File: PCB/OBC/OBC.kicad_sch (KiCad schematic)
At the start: 1 part, among them U1 STM32F405RGTx

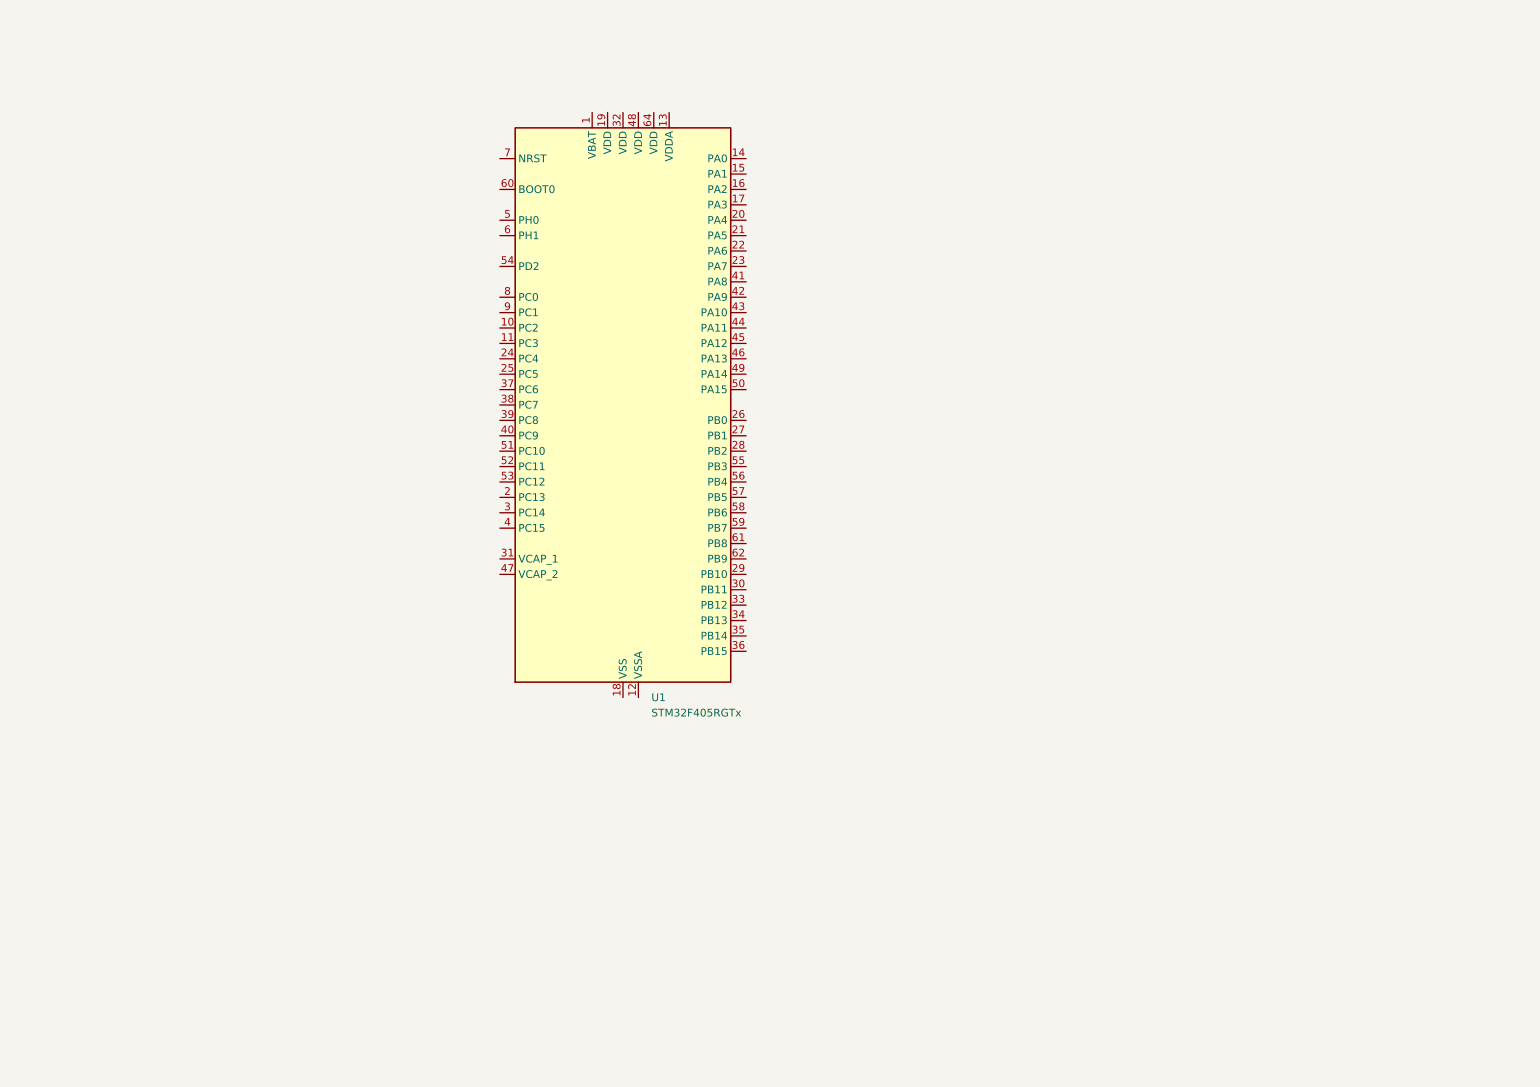
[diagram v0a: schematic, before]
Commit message: Adding LDO and Stm32F4
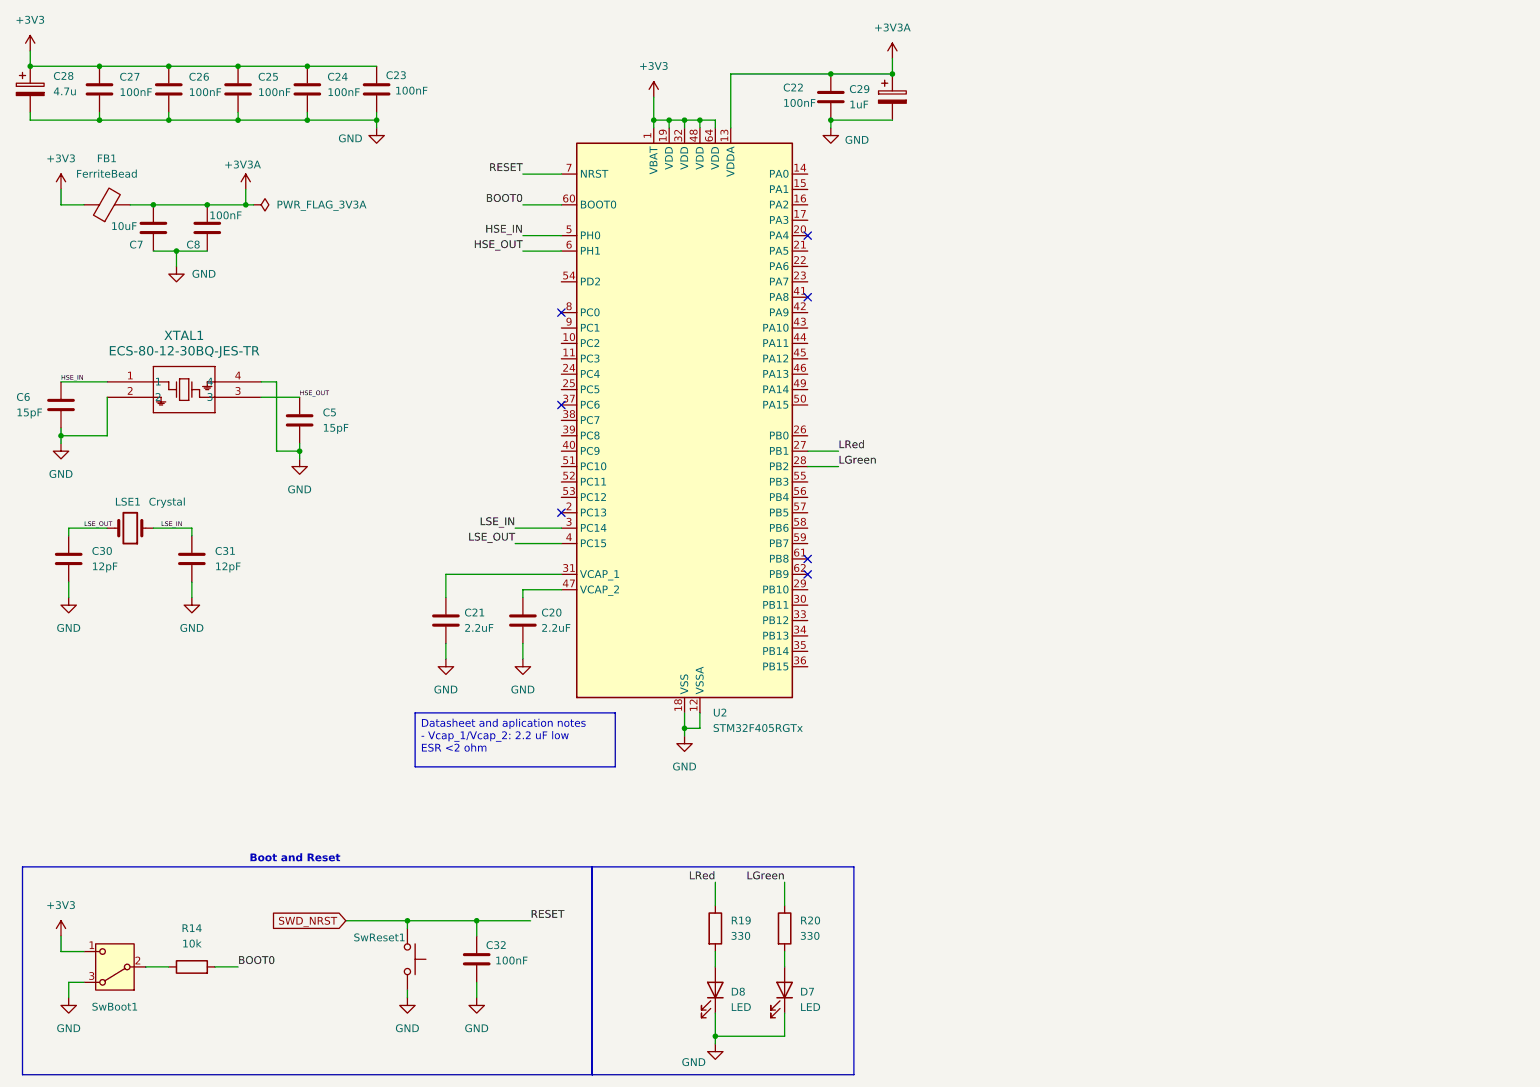
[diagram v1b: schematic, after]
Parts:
- removed U1: STM32F405RGTx, Package_QFP:LQFP-64_10x10mm_P0.5mm, symbol MCU_ST_STM32F4:STM32F405RGTx
- added C20, C21: 2.2uF, Capacitor_SMD:C_0805_2012Metric_Pad1.18x1.45mm_HandSolder, symbol Device:C
- added C22, C23, C25, C27, C32: 100nF, Capacitor_SMD:C_0603_1608Metric_Pad1.08x0.95mm_HandSolder, symbol Device:C
- added C24, C26, C8: 100nF, Capacitor_SMD:C_0805_2012Metric_Pad1.18x1.45mm_HandSolder, symbol Device:C
- added C28: 4.7u, Capacitor_SMD:C_0805_2012Metric_Pad1.18x1.45mm_HandSolder, symbol Device:C_Polarized
- added C29: 1uF, Capacitor_SMD:C_0805_2012Metric_Pad1.18x1.45mm_HandSolder, symbol Device:C_Polarized
- added C30, C31: 12pF, Capacitor_SMD:C_0603_1608Metric_Pad1.08x0.95mm_HandSolder, symbol Device:C
- added C5, C6: 15pF, Capacitor_SMD:C_0603_1608Metric_Pad1.08x0.95mm_HandSolder, symbol Device:C
- added C7: 10uF, Capacitor_SMD:C_0805_2012Metric_Pad1.18x1.45mm_HandSolder, symbol Device:C
- added D7, D8: LED, LED_SMD:LED_0805_2012Metric_Pad1.15x1.40mm_HandSolder, symbol Device:LED
- added FB1: FerriteBead, Capacitor_SMD:C_0805_2012Metric_Pad1.18x1.45mm_HandSolder, symbol Device:FerriteBead
- added LSE1: Crystal, ndx32khz:XTAL_NX3215SA_NDK, symbol Device:Crystal
- added R14: 10k, Resistor_SMD:R_0805_2012Metric_Pad1.20x1.40mm_HandSolder, symbol Device:R
- added R19, R20: 330, Resistor_SMD:R_0805_2012Metric_Pad1.20x1.40mm_HandSolder, symbol Device:R
- added SwBoot1: SW_Nidec_CAS-120A1, Button_Switch_SMD:Nidec_Copal_CAS-120A, symbol Switch:SW_Nidec_CAS-120A1
- added SwReset1: SW_Push, Button_Switch_SMD:SW_Push_SPST_NO_Alps_SKRK, symbol Switch:SW_Push
- added U2: STM32F405RGTx, Package_QFP:LQFP-64_10x10mm_P0.5mm, symbol MCU_ST_STM32F4:STM32F405RGTx
- added XTAL1: ECS-80-12-30BQ-JES-TR, ESCMHZ:ECS-80-12_ECS, symbol ESC8Mhz:ECS-80-12-30BQ-JES-TR
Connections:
- new net: D7.2 (A), R20.2
- new net: C20.1, U2.47 (VCAP_2)
- new net: R14.1, SwBoot1.2 (B)
- new net: D8.2 (A), R19.2
- new net: C21.1, U2.31 (VCAP_1)
- new net +3V3: C23.1, C24.1, C25.1, C26.1, C27.1, C28.1, FB1.1, SwBoot1.1 (C), U2.1 (VBAT), U2.19 (VDD), U2.32 (VDD), U2.48 (VDD), U2.64 (VDD)
- new net +3V3A: C22.1, C29.1, C7.2, C8.2, FB1.2, U2.13 (VDDA)
- new net BOOT0: R14.2, U2.60 (BOOT0)
- new net GND: C20.2, C21.2, C22.2, C23.2, C24.2, C25.2, C26.2, C27.2, C28.2, C29.2, C30.2, C31.2, C32.2, C5.2, C6.2, C7.1, C8.1, D7.1 (K), D8.1 (K), SwBoot1.3 (A), SwReset1.1, U2.12 (VSSA), U2.18 (VSS), U2.63 (VSS), XTAL1.2, XTAL1.4
- new net HSE_IN: C6.1, U2.5 (PH0), XTAL1.1
- new net HSE_OUT: C5.1, U2.6 (PH1), XTAL1.3
- new net LGreen: R20.1, U2.28 (PB2)
- new net LRed: R19.1, U2.27 (PB1)
- new net LSE_IN: C31.1, LSE1.1, U2.3 (PC14)
- new net LSE_OUT: C30.1, LSE1.2, U2.4 (PC15)
- new net SWD_NRST: C32.1, SwReset1.2, U2.7 (NRST)
- no-connect marks 0 -> 7
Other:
- note added: "Boot and Reset"

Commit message: CubeMx and schematic
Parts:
- added D3: D_Schottky, Diode_SMD:D_SOD-323_HandSoldering, symbol Device:D_Schottky
- added J7: USB_C_Receptacle_USB2.0_16P, USB4940-00-A:USB494000A, symbol Connector:USB_C_Receptacle_USB2.0_16P
- added R15, R16: 5k1, Resistor_SMD:R_0805_2012Metric_Pad1.20x1.40mm_HandSolder, symbol Device:R
- added U1: TLV77533PDBVR, SOT-23-5_1P75X3P05_TEX, symbol TLV77533:TLV77533PDBVR
- added U5: USBLC6-2SC6, Package_TO_SOT_SMD:SOT-23-6, symbol Power_Protection:USBLC6-2SC6
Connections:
- net GND: now also J7.A1 (GND), J7.A12 (GND), J7.B1 (GND), J7.B12 (GND), J7.S1 (SHIELD), R15.2, R16.2, U5.2 (GND)
- new net: D3.2 (A), J7.A4 (VBUS), J7.A9 (VBUS), J7.B4 (VBUS), J7.B9 (VBUS)
- new net CC1: J7.A5 (CC1), R15.1
- new net CC2: J7.B5 (CC2), R16.1
- new net D+: J7.A6 (D+), J7.B6 (D+), U5.3 (I/O2)
- new net D-: J7.A7 (D-), J7.B7 (D-), U5.1 (I/O1)
- new net LDO_USB: D3.1 (K), U5.5 (VBUS)
- new net USB_D+: U5.4 (I/O2)
- new net USB_D-: U5.6 (I/O1)
- no-connect marks 7 -> 9

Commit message: minors chages
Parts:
- removed U1: TLV77533PDBVR, SOT-23-5_1P75X3P05_TEX, symbol TLV77533:TLV77533PDBVR

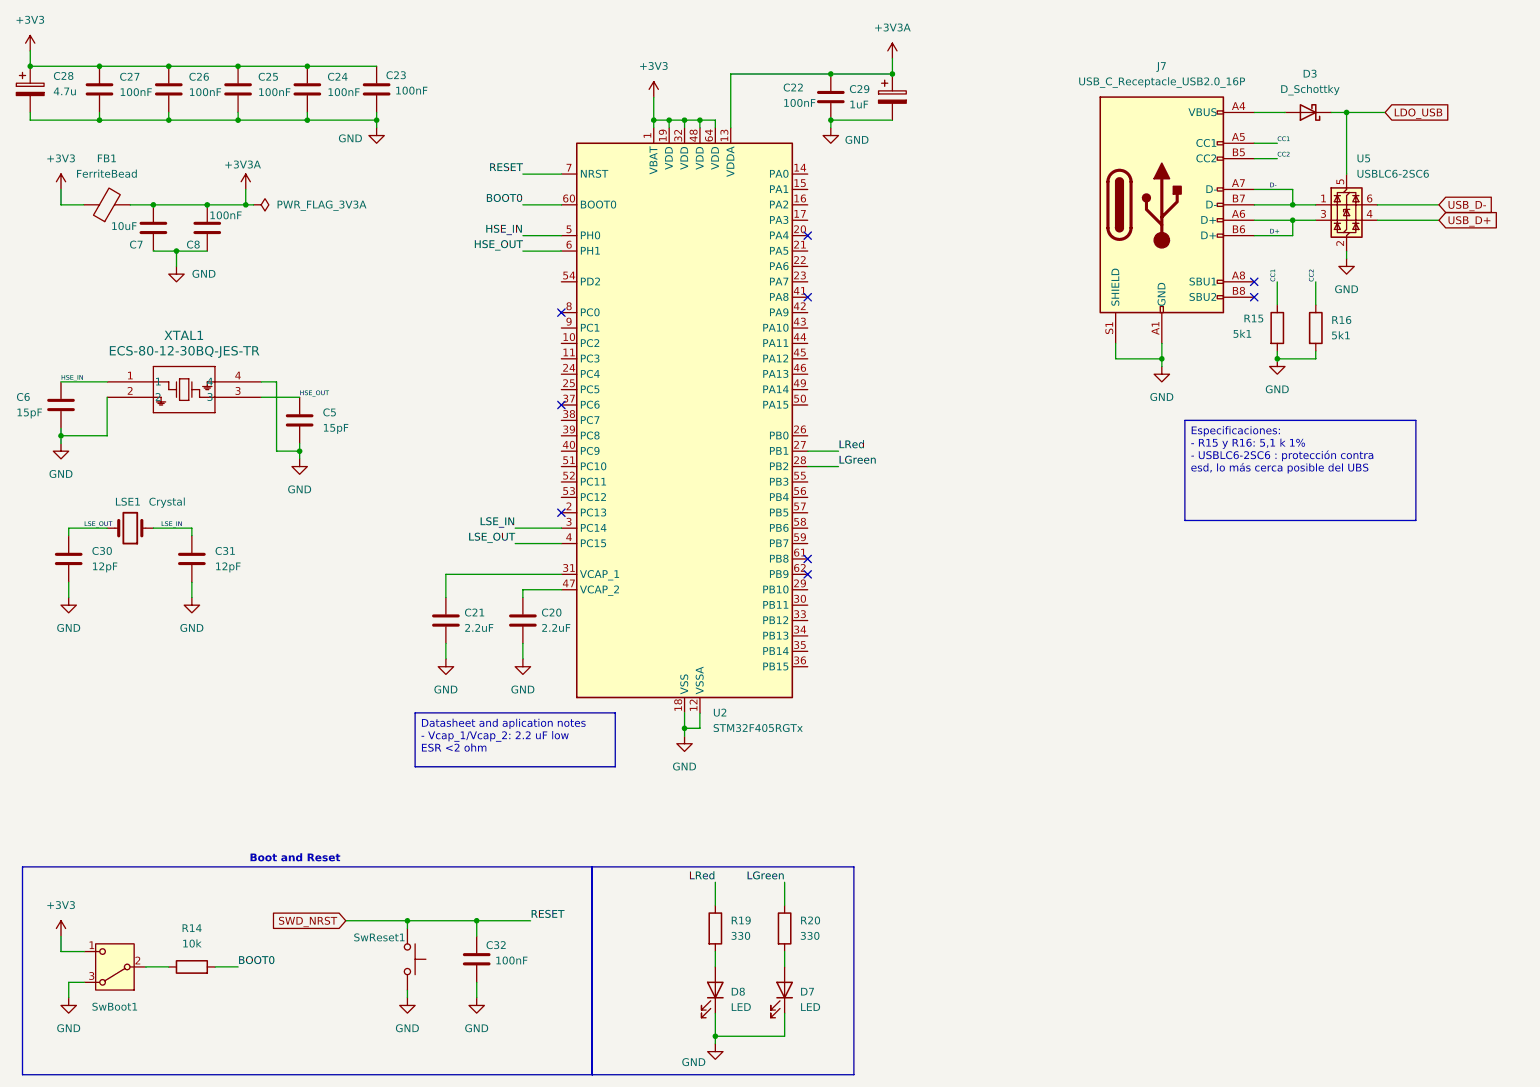
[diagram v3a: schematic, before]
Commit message: Adding the COMS and Reset MCU
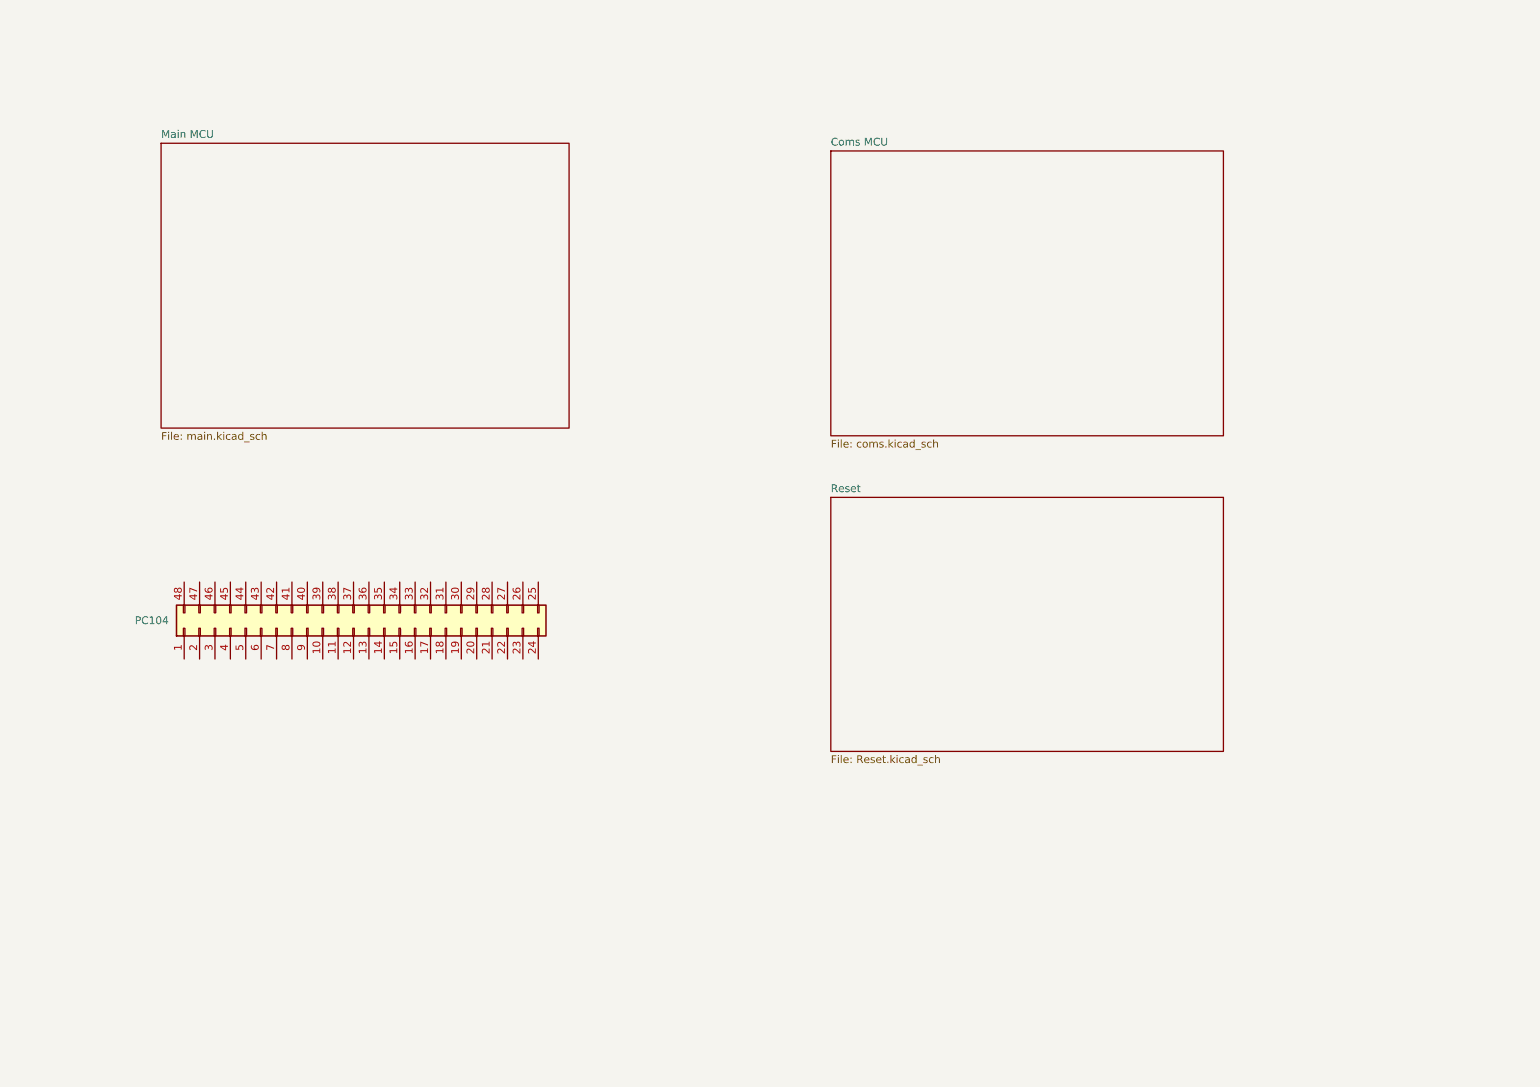
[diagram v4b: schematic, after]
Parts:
- removed C20, C21: 2.2uF, Capacitor_SMD:C_0805_2012Metric_Pad1.18x1.45mm_HandSolder, symbol Device:C
- removed C22, C23, C25, C27, C32: 100nF, Capacitor_SMD:C_0603_1608Metric_Pad1.08x0.95mm_HandSolder, symbol Device:C
- removed C24, C26, C8: 100nF, Capacitor_SMD:C_0805_2012Metric_Pad1.18x1.45mm_HandSolder, symbol Device:C
- removed C28: 4.7u, Capacitor_SMD:C_0805_2012Metric_Pad1.18x1.45mm_HandSolder, symbol Device:C_Polarized
- removed C29: 1uF, Capacitor_SMD:C_0805_2012Metric_Pad1.18x1.45mm_HandSolder, symbol Device:C_Polarized
- removed C30, C31: 12pF, Capacitor_SMD:C_0603_1608Metric_Pad1.08x0.95mm_HandSolder, symbol Device:C
- removed C5, C6: 15pF, Capacitor_SMD:C_0603_1608Metric_Pad1.08x0.95mm_HandSolder, symbol Device:C
- removed C7: 10uF, Capacitor_SMD:C_0805_2012Metric_Pad1.18x1.45mm_HandSolder, symbol Device:C
- removed D3: D_Schottky, Diode_SMD:D_SOD-323_HandSoldering, symbol Device:D_Schottky
- removed D7, D8: LED, LED_SMD:LED_0805_2012Metric_Pad1.15x1.40mm_HandSolder, symbol Device:LED
- removed FB1: FerriteBead, Capacitor_SMD:C_0805_2012Metric_Pad1.18x1.45mm_HandSolder, symbol Device:FerriteBead
- removed J7: USB_C_Receptacle_USB2.0_16P, USB4940-00-A:USB494000A, symbol Connector:USB_C_Receptacle_USB2.0_16P
- removed LSE1: Crystal, ndx32khz:XTAL_NX3215SA_NDK, symbol Device:Crystal
- removed R14: 10k, Resistor_SMD:R_0805_2012Metric_Pad1.20x1.40mm_HandSolder, symbol Device:R
- removed R15, R16: 5k1, Resistor_SMD:R_0805_2012Metric_Pad1.20x1.40mm_HandSolder, symbol Device:R
- removed R19, R20: 330, Resistor_SMD:R_0805_2012Metric_Pad1.20x1.40mm_HandSolder, symbol Device:R
- removed SwBoot1: SW_Nidec_CAS-120A1, Button_Switch_SMD:Nidec_Copal_CAS-120A, symbol Switch:SW_Nidec_CAS-120A1
- removed SwReset1: SW_Push, Button_Switch_SMD:SW_Push_SPST_NO_Alps_SKRK, symbol Switch:SW_Push
- removed U2: STM32F405RGTx, Package_QFP:LQFP-64_10x10mm_P0.5mm, symbol MCU_ST_STM32F4:STM32F405RGTx
- removed U5: USBLC6-2SC6, Package_TO_SOT_SMD:SOT-23-6, symbol Power_Protection:USBLC6-2SC6
- removed XTAL1: ECS-80-12-30BQ-JES-TR, ESCMHZ:ECS-80-12_ECS, symbol ESC8Mhz:ECS-80-12-30BQ-JES-TR
- added PC104: Conn_02x24_Counter_Clockwise, Connector_PinHeader_2.54mm:PinHeader_2x24_P2.54mm_Vertical, symbol Connector_Generic:Conn_02x24_Counter_Clockwise
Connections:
- no-connect marks 9 -> 0
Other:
- added sheet Coms MCU (coms.kicad_sch)
- added sheet Main MCU (main.kicad_sch)
- added sheet Reset (Reset.kicad_sch)
- note removed: "Boot and Reset"
